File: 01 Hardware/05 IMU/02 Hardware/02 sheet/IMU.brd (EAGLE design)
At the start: 100 x 80 mm, 1 part, among them U2 RASPBERRY_PICOTH

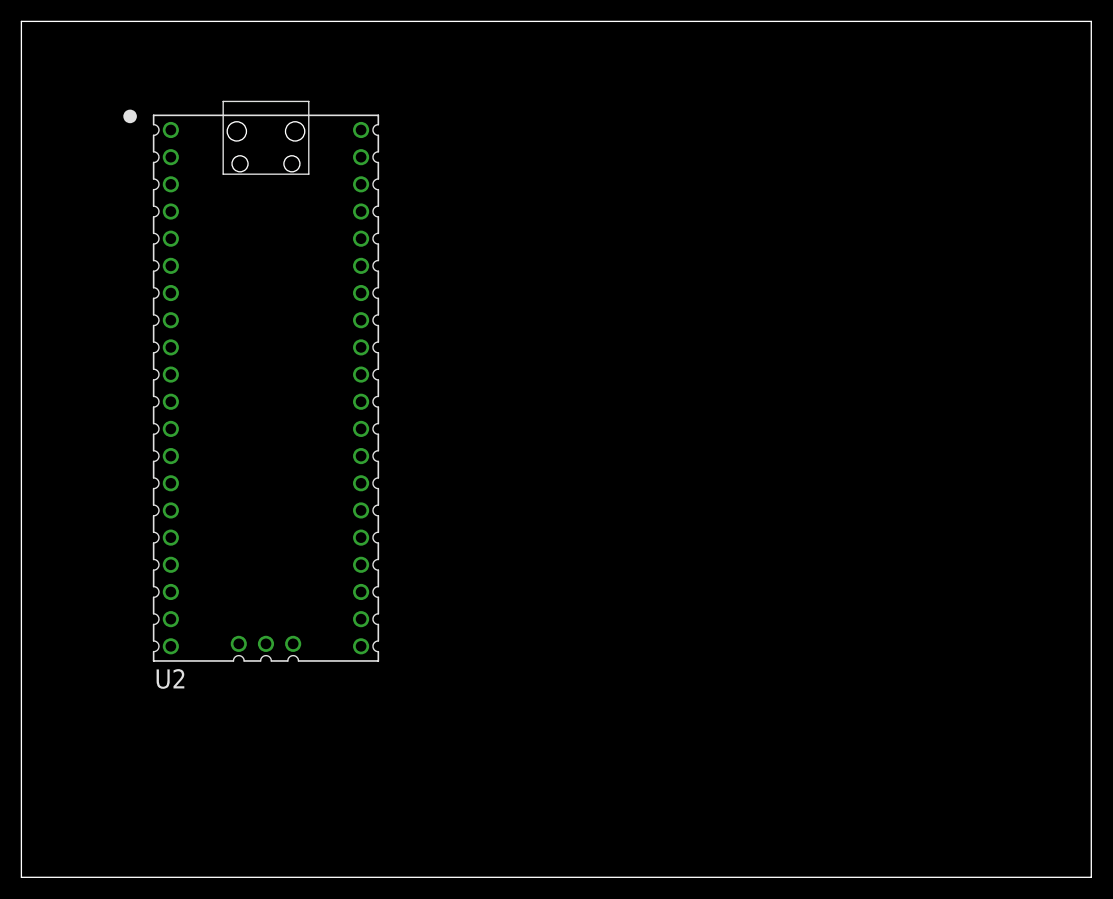
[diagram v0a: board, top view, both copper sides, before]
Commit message: USV Slave Template
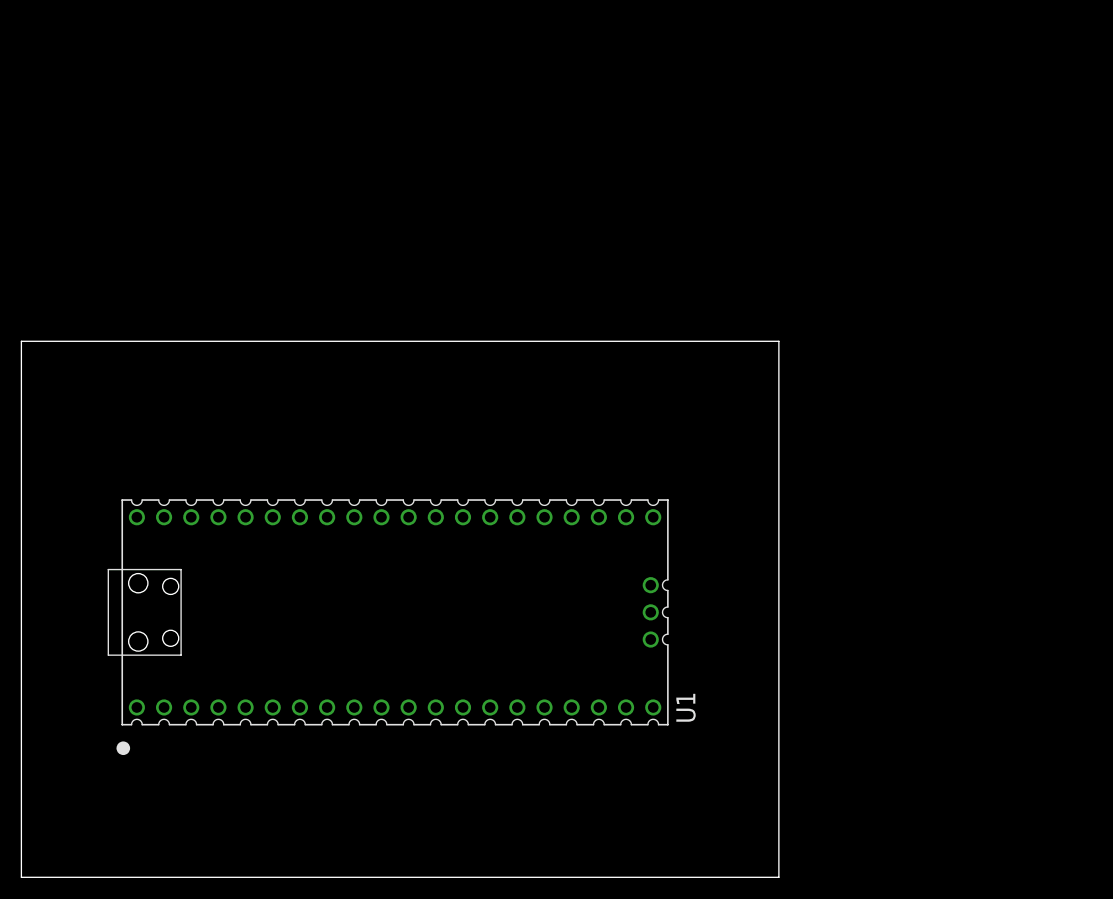
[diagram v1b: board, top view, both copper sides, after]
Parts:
- removed U2: RASPBERRY_PICOTH, RpiPico:PICO-PKG-TH
- added U1: RASPBERRY_PICOTH, RpiPico:PICO-PKG-TH
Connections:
- net 3V3(OUT): now also U1.36; no longer U2.36
- net GND: now also U1.13, U1.18, U1.23, U1.28, U1.3, U1.33, U1.38, U1.8; no longer U2.13, U2.18, U2.23, U2.28, U2.3, U2.33, U2.38, U2.8
- net SWGND: now also U1.42; no longer U2.42
- net VBUS: now also U1.40; no longer U2.40
- net VSYS: now also U1.39; no longer U2.39
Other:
- board size 100 x 80 mm -> 70.8 x 50.1 mm
